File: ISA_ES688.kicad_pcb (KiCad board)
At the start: 4 copper layers, 104.1 x 99.1 mm, 105 parts, among them J1 LINE IN, J10 Vol. Btns, J11 ISA BUS, J2 MIC, J3 Joystick/MIDI, J5 Wavetable, J7 SPKR OUT, J8 LINE OUT, U1 L78L05, U2 74LS138, U3 ES1868F, U4 93LC66, U7 LM1877, Y1 14.318Mhz

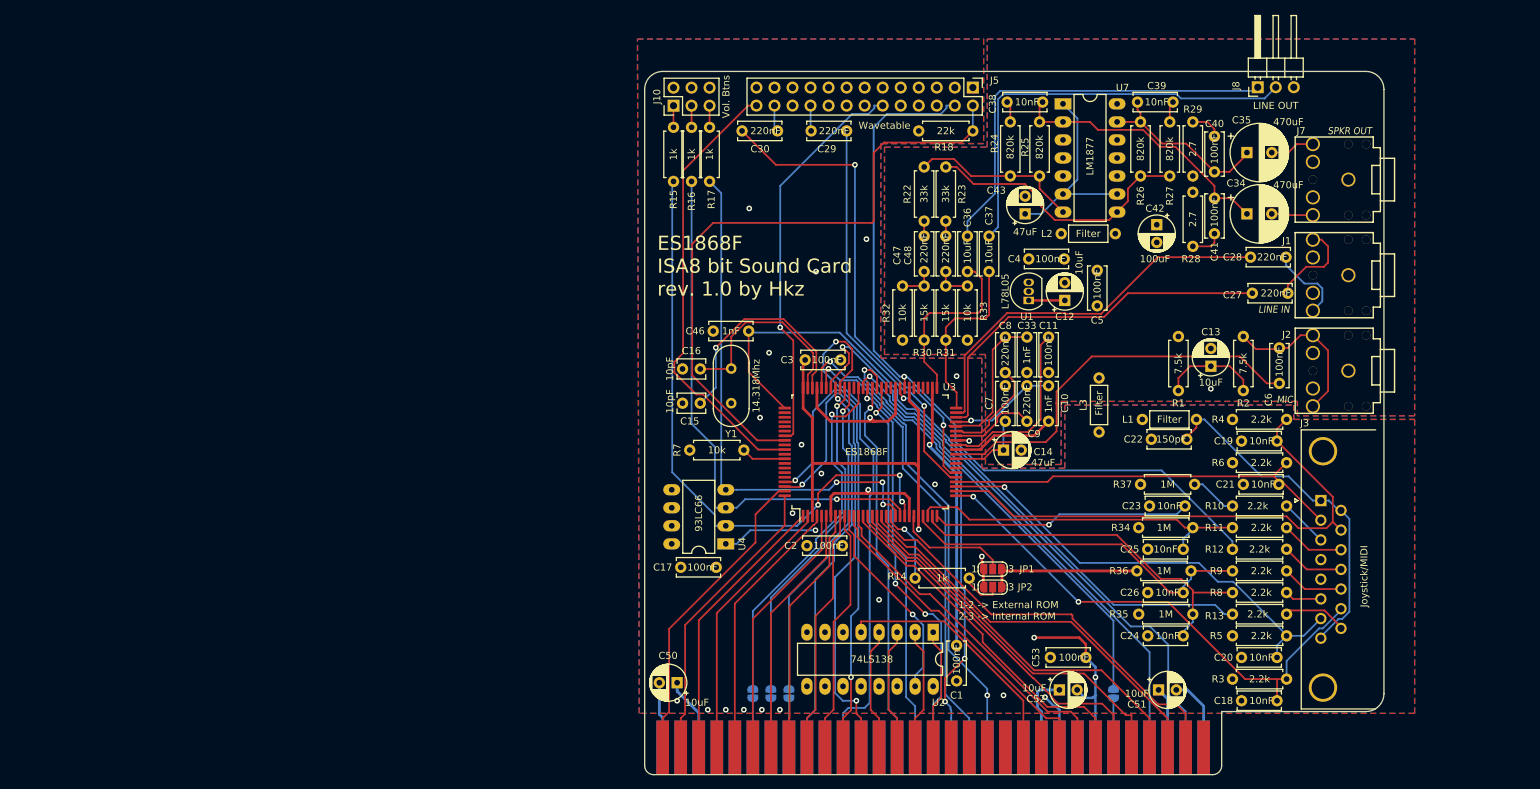
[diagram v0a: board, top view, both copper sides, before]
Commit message: Begin laying out parts
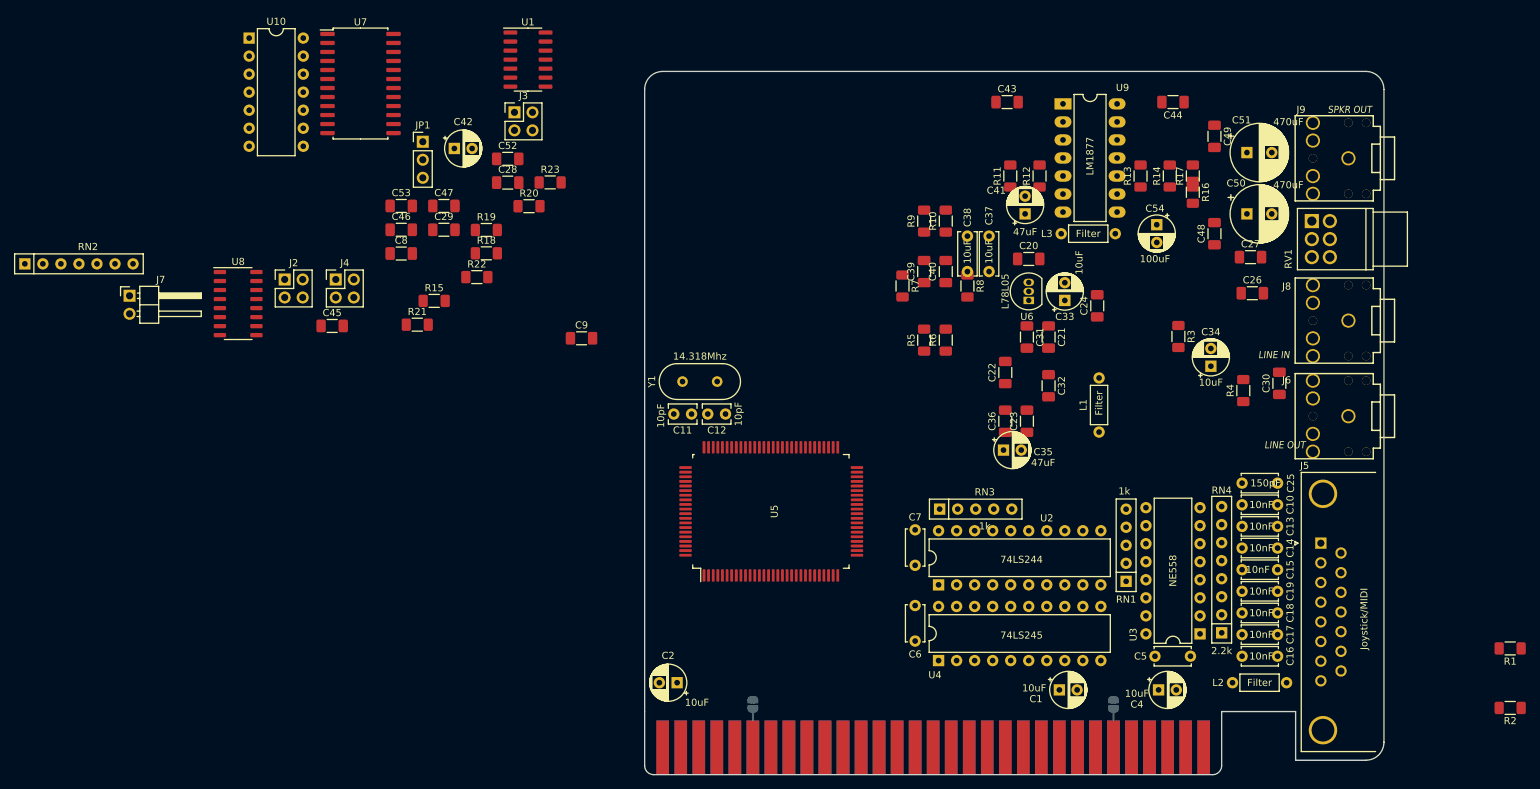
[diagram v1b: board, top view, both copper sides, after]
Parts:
- removed the C20 at (294.9, 186.7)
- removed the C21 at (295.1, 162.3)
- removed the C23 at (281.9, 165.4)
- removed the C24 at (281.7, 183.6)
- removed the C25 at (281.7, 171.4)
- removed the C26 at (281.7, 177.5)
- removed the C30 at (224.5, 112.5)
- removed J10: Vol. Btns, Connector_PinHeader_2.54mm:PinHeader_2x03_P2.54mm_Vertical
- removed the J5 at (257.0, 106.4)
- removed the J8 at (297.2, 106.4)
- removed JP4: ~DACK2~ Jumper, Jumper:SolderJumper-2_P1.3mm_Open_RoundedPad1.0x1.5mm
- removed JP5: IRQ3 Jumper, Jumper:SolderJumper-2_P1.3mm_Open_RoundedPad1.0x1.5mm
- removed JP6: IRQ4 Jumper, Jumper:SolderJumper-2_P1.3mm_Open_RoundedPad1.0x1.5mm
- removed the R10 at (301.2, 165.4)
- removed the R11 at (301.2, 168.4)
- removed the R14 at (256.5, 175.5)
- removed the R16 at (217.4, 119.6)
- removed the R17 at (220.0, 119.6)
- removed the R3 at (301.2, 189.7)
- removed R34, R35, R36, R37: 1M, Resistor_THT:R_Axial_DIN0207_L6.3mm_D2.5mm_P7.62mm_Horizontal
- removed the R4 at (301.2, 153.2)
- removed the R5 at (301.2, 183.6)
- removed the R6 at (301.2, 159.3)
- removed the R7 at (224.8, 157.5)
- removed the R8 at (301.2, 177.5)
- removed the R9 at (301.2, 174.5)
- added C10: 10nF, Capacitor_THT:C_Disc_D5.0mm_W2.5mm_P5.00mm, F.Cu at (300.0, 165.2)
- added C13: 10nF, Capacitor_THT:C_Disc_D5.0mm_W2.5mm_P5.00mm, F.Cu at (300.0, 168.2)
- added C14: 10nF, Capacitor_THT:C_Disc_D5.0mm_W2.5mm_P5.00mm, F.Cu at (300.0, 171.3)
- added C15: 10nF, Capacitor_THT:C_Disc_D5.0mm_W2.5mm_P5.00mm, F.Cu at (300.0, 174.3)
- added C16: 10nF, Capacitor_THT:C_Disc_D5.0mm_W2.5mm_P5.00mm, F.Cu at (300.0, 186.5)
- added C28: 220nF, Capacitor_SMD:C_1206_3216Metric_Pad1.33x1.80mm_HandSolder, F.Cu at (191.5, 119.8)
- added C42: 10uF, Capacitor_THT:CP_Radial_D5.0mm_P2.50mm, F.Cu at (184.0, 115.0)
- added C45: 2.7nF, Capacitor_SMD:C_1206_3216Metric_Pad1.33x1.80mm_HandSolder, F.Cu at (166.8, 140.0)
- added C46: 2.7nF, Capacitor_SMD:C_1206_3216Metric_Pad1.33x1.80mm_HandSolder, F.Cu at (176.5, 126.4)
- added C47: 33-68pF, Capacitor_SMD:C_1206_3216Metric_Pad1.33x1.80mm_HandSolder, F.Cu at (182.5, 123.1)
- added C52: 5nF, Capacitor_SMD:C_1206_3216Metric_Pad1.33x1.80mm_HandSolder, F.Cu at (191.5, 116.5)
- added C8: 10nF, Capacitor_SMD:C_1206_3216Metric_Pad1.33x1.80mm_HandSolder, F.Cu at (176.5, 129.8)
- added J2: Interrupt Select, Connector_PinHeader_2.54mm:PinHeader_2x02_P2.54mm_Vertical, F.Cu at (160.1, 133.4)
- added J3: Address Select, Connector_PinHeader_2.54mm:PinHeader_2x02_P2.54mm_Vertical, F.Cu at (192.5, 109.9)
- added J4: DMA Select, Connector_PinHeader_2.54mm:PinHeader_2x02_P2.54mm_Vertical, F.Cu at (167.3, 133.4)
- added J7: MIC, Connector_PinHeader_2.54mm:PinHeader_1x02_P2.54mm_Horizontal, F.Cu at (138.3, 135.7)
- added R19: 2.2k, Resistor_SMD:R_1206_3216Metric_Pad1.30x1.75mm_HandSolder, F.Cu at (188.5, 126.5)
- added R20: 10k, Resistor_SMD:R_1206_3216Metric_Pad1.30x1.75mm_HandSolder, F.Cu at (194.5, 123.1)
- added R21: 2.2k, Resistor_SMD:R_1206_3216Metric_Pad1.30x1.75mm_HandSolder, F.Cu at (178.8, 139.8)
- added R22: 10k, Resistor_SMD:R_1206_3216Metric_Pad1.30x1.75mm_HandSolder, F.Cu at (187.2, 133.1)
- added R23: 10k, Resistor_SMD:R_1206_3216Metric_Pad1.30x1.75mm_HandSolder, F.Cu at (197.5, 119.8)
- added RN1: 1k, Resistor_THT:R_Array_SIP5, F.Cu at (278.6, 176.0)
- added RN2: R_Network06, Resistor_THT:R_Array_SIP7, F.Cu at (123.5, 131.2)
- added RN3: 1k, Resistor_THT:R_Array_SIP5, F.Cu at (252.4, 165.8)
- added RN4: 2.2k, Resistor_THT:R_Array_SIP8, F.Cu at (292.1, 183.2)
- added RV1: Volume Knob, Volume_Pot:PTD902, F.Cu at (304.8, 125.2)
- added U1: 74LS14, Package_SO:SOIC-14_3.9x8.7mm_P1.27mm, F.Cu at (194.4, 102.5)
- added U10: LM3403, Package_DIP:DIP-14_W7.62mm, F.Cu at (155.1, 99.4)
- added U5: ES688F, Package_QFP:LQFP-14x20mm_P0.5mm, F.Cu at (228.6, 166.1)
- added U7: YMF262-M, Package_SO:SOIC-24W_7.5x15.4mm_P1.27mm, F.Cu at (170.8, 105.8)
- added U8: YAC512, Package_SO:SO-16_3.9x9.9mm_P1.27mm, F.Cu at (153.6, 136.8)
- C17: value 100nF -> 10nF; footprint Capacitor_THT:C_Disc_D6.0mm_W2.5mm_P5.00mm -> Capacitor_THT:C_Disc_D5.0mm_W2.5mm_P5.00mm
- C18, C19: footprint Capacitor_THT:C_Disc_D6.0mm_W2.5mm_P5.00mm -> Capacitor_THT:C_Disc_D5.0mm_W2.5mm_P5.00mm
- C20: renamed from C4; footprint Capacitor_THT:C_Disc_D6.0mm_W2.5mm_P5.00mm -> Capacitor_SMD:C_1206_3216Metric_Pad1.33x1.80mm_HandSolder
- C21: renamed from C11; footprint Capacitor_THT:C_Disc_D6.0mm_W2.5mm_P5.00mm -> Capacitor_SMD:C_1206_3216Metric_Pad1.33x1.80mm_HandSolder
- C22: renamed from C8; footprint Capacitor_THT:C_Disc_D6.0mm_W2.5mm_P5.00mm -> Capacitor_SMD:C_1206_3216Metric_Pad1.33x1.80mm_HandSolder
- C23: renamed from C9; footprint Capacitor_THT:C_Disc_D6.0mm_W2.5mm_P5.00mm -> Capacitor_SMD:C_1206_3216Metric_Pad1.33x1.80mm_HandSolder
- C24: renamed from C5; footprint Capacitor_THT:C_Disc_D6.0mm_W2.5mm_P5.00mm -> Capacitor_SMD:C_1206_3216Metric_Pad1.33x1.80mm_HandSolder
- C25: renamed from C22; footprint Capacitor_THT:C_Disc_D6.0mm_W2.5mm_P5.00mm -> Capacitor_THT:C_Disc_D5.0mm_W2.5mm_P5.00mm
- C26: renamed from C27; footprint Capacitor_THT:C_Disc_D6.0mm_W2.5mm_P5.00mm -> Capacitor_SMD:C_1206_3216Metric_Pad1.33x1.80mm_HandSolder
- C27: renamed from C28; footprint Capacitor_THT:C_Disc_D6.0mm_W2.5mm_P5.00mm -> Capacitor_SMD:C_1206_3216Metric_Pad1.33x1.80mm_HandSolder
- C29: footprint Capacitor_THT:C_Disc_D6.0mm_W2.5mm_P5.00mm -> Capacitor_SMD:C_1206_3216Metric_Pad1.33x1.80mm_HandSolder
- C30: renamed from C6; footprint Capacitor_THT:C_Disc_D6.0mm_W2.5mm_P5.00mm -> Capacitor_SMD:C_1206_3216Metric_Pad1.33x1.80mm_HandSolder
- C31: renamed from C33; footprint Capacitor_THT:C_Disc_D6.0mm_W2.5mm_P5.00mm -> Capacitor_SMD:C_1206_3216Metric_Pad1.33x1.80mm_HandSolder
- C32: renamed from C10; footprint Capacitor_THT:C_Disc_D6.0mm_W2.5mm_P5.00mm -> Capacitor_SMD:C_1206_3216Metric_Pad1.33x1.80mm_HandSolder
- C36: renamed from C7; footprint Capacitor_THT:C_Disc_D6.0mm_W2.5mm_P5.00mm -> Capacitor_SMD:C_1206_3216Metric_Pad1.33x1.80mm_HandSolder
- C39: renamed from C47; footprint Capacitor_THT:C_Disc_D6.0mm_W2.5mm_P5.00mm -> Capacitor_SMD:C_1206_3216Metric_Pad1.33x1.80mm_HandSolder
- C40: renamed from C48; footprint Capacitor_THT:C_Disc_D6.0mm_W2.5mm_P5.00mm -> Capacitor_SMD:C_1206_3216Metric_Pad1.33x1.80mm_HandSolder
- C43: renamed from C38; footprint Capacitor_THT:C_Disc_D6.0mm_W2.5mm_P5.00mm -> Capacitor_SMD:C_1206_3216Metric_Pad1.33x1.80mm_HandSolder
- C44: renamed from C39; footprint Capacitor_THT:C_Disc_D6.0mm_W2.5mm_P5.00mm -> Capacitor_SMD:C_1206_3216Metric_Pad1.33x1.80mm_HandSolder
- C48: renamed from C41; footprint Capacitor_THT:C_Disc_D6.0mm_W2.5mm_P5.00mm -> Capacitor_SMD:C_1206_3216Metric_Pad1.33x1.80mm_HandSolder
- C49: renamed from C40; footprint Capacitor_THT:C_Disc_D6.0mm_W2.5mm_P5.00mm -> Capacitor_SMD:C_1206_3216Metric_Pad1.33x1.80mm_HandSolder
- C5: renamed from C1; footprint Capacitor_THT:C_Disc_D6.0mm_W2.5mm_P5.00mm -> Capacitor_THT:C_Disc_D5.0mm_W2.5mm_P5.00mm
- C53: value 100nF -> 5nF; footprint Capacitor_THT:C_Disc_D6.0mm_W2.5mm_P5.00mm -> Capacitor_SMD:C_1206_3216Metric_Pad1.33x1.80mm_HandSolder
- C6: renamed from C2; footprint Capacitor_THT:C_Disc_D6.0mm_W2.5mm_P5.00mm -> Capacitor_THT:C_Disc_D5.0mm_W2.5mm_P5.00mm
- C7: renamed from C3; footprint Capacitor_THT:C_Disc_D6.0mm_W2.5mm_P5.00mm -> Capacitor_THT:C_Disc_D5.0mm_W2.5mm_P5.00mm
- C9: renamed from C46; footprint Capacitor_THT:C_Disc_D6.0mm_W2.5mm_P5.00mm -> Capacitor_SMD:C_1206_3216Metric_Pad1.33x1.80mm_HandSolder
- J6: renamed from J2; value MIC -> LINE OUT
- JP1: value Intl. ROM 1 -> Emulation Mode; footprint Jumper:SolderJumper-3_P1.3mm_Open_RoundedPad1.0x1.5mm_NumberLabels -> Connector_PinHeader_2.54mm:PinHeader_1x03_P2.54mm_Vertical
- JP2: value Intl. ROM 2 -> ~DRQ2~ Jumper; footprint Jumper:SolderJumper-3_P1.3mm_Open_RoundedPad1.0x1.5mm_NumberLabels -> Jumper:SolderJumper-2_P1.3mm_Open_RoundedPad1.0x1.5mm; moved to B.Cu
- JP3: value ~DRQ2~ Jumper -> ~DACK2~ Jumper
- R1: renamed from R12; footprint Resistor_THT:R_Axial_DIN0207_L6.3mm_D2.5mm_P7.62mm_Horizontal -> Resistor_SMD:R_1206_3216Metric_Pad1.30x1.75mm_HandSolder
- R10: renamed from R23; footprint Resistor_THT:R_Axial_DIN0207_L6.3mm_D2.5mm_P7.62mm_Horizontal -> Resistor_SMD:R_1206_3216Metric_Pad1.30x1.75mm_HandSolder
- R11: renamed from R24; footprint Resistor_THT:R_Axial_DIN0207_L6.3mm_D2.5mm_P7.62mm_Horizontal -> Resistor_SMD:R_1206_3216Metric_Pad1.30x1.75mm_HandSolder
- R12: renamed from R25; footprint Resistor_THT:R_Axial_DIN0207_L6.3mm_D2.5mm_P7.62mm_Horizontal -> Resistor_SMD:R_1206_3216Metric_Pad1.30x1.75mm_HandSolder
- R13: renamed from R26; footprint Resistor_THT:R_Axial_DIN0207_L6.3mm_D2.5mm_P7.62mm_Horizontal -> Resistor_SMD:R_1206_3216Metric_Pad1.30x1.75mm_HandSolder
- R14: renamed from R27; footprint Resistor_THT:R_Axial_DIN0207_L6.3mm_D2.5mm_P7.62mm_Horizontal -> Resistor_SMD:R_1206_3216Metric_Pad1.30x1.75mm_HandSolder
- R15: value 1k -> 33; footprint Resistor_THT:R_Axial_DIN0207_L6.3mm_D2.5mm_P7.62mm_Horizontal -> Resistor_SMD:R_1206_3216Metric_Pad1.30x1.75mm_HandSolder
- R16: renamed from R28; footprint Resistor_THT:R_Axial_DIN0207_L6.3mm_D2.5mm_P7.62mm_Horizontal -> Resistor_SMD:R_1206_3216Metric_Pad1.30x1.75mm_HandSolder
- R17: renamed from R29; footprint Resistor_THT:R_Axial_DIN0207_L6.3mm_D2.5mm_P7.62mm_Horizontal -> Resistor_SMD:R_1206_3216Metric_Pad1.30x1.75mm_HandSolder
- R18: value 22k -> 10k; footprint Resistor_THT:R_Axial_DIN0207_L6.3mm_D2.5mm_P7.62mm_Horizontal -> Resistor_SMD:R_1206_3216Metric_Pad1.30x1.75mm_HandSolder
- R2: renamed from R13; footprint Resistor_THT:R_Axial_DIN0207_L6.3mm_D2.5mm_P7.62mm_Horizontal -> Resistor_SMD:R_1206_3216Metric_Pad1.30x1.75mm_HandSolder
- R3: renamed from R1; footprint Resistor_THT:R_Axial_DIN0207_L6.3mm_D2.5mm_P7.62mm_Horizontal -> Resistor_SMD:R_1206_3216Metric_Pad1.30x1.75mm_HandSolder
- R4: renamed from R2; footprint Resistor_THT:R_Axial_DIN0207_L6.3mm_D2.5mm_P7.62mm_Horizontal -> Resistor_SMD:R_1206_3216Metric_Pad1.30x1.75mm_HandSolder
- R5: renamed from R30; footprint Resistor_THT:R_Axial_DIN0207_L6.3mm_D2.5mm_P7.62mm_Horizontal -> Resistor_SMD:R_1206_3216Metric_Pad1.30x1.75mm_HandSolder
- R6: renamed from R31; footprint Resistor_THT:R_Axial_DIN0207_L6.3mm_D2.5mm_P7.62mm_Horizontal -> Resistor_SMD:R_1206_3216Metric_Pad1.30x1.75mm_HandSolder
- R7: renamed from R32; footprint Resistor_THT:R_Axial_DIN0207_L6.3mm_D2.5mm_P7.62mm_Horizontal -> Resistor_SMD:R_1206_3216Metric_Pad1.30x1.75mm_HandSolder
- R8: renamed from R33; footprint Resistor_THT:R_Axial_DIN0207_L6.3mm_D2.5mm_P7.62mm_Horizontal -> Resistor_SMD:R_1206_3216Metric_Pad1.30x1.75mm_HandSolder
- R9: renamed from R22; footprint Resistor_THT:R_Axial_DIN0207_L6.3mm_D2.5mm_P7.62mm_Horizontal -> Resistor_SMD:R_1206_3216Metric_Pad1.30x1.75mm_HandSolder
- U2: value 74LS138 -> 74LS244; footprint Package_DIP:DIP-16_W7.62mm_LongPads -> Package_DIP:DIP-20_W7.62mm
- U3: value ES1868F -> NE558; footprint Package_QFP:LQFP-14x20mm_P0.5mm -> Package_DIP:DIP-16_W7.62mm
- U4: value 93LC66 -> 74LS245; footprint Package_DIP:DIP-8_W7.62mm_LongPads -> Package_DIP:DIP-20_W7.62mm
- moved C53 111.4 mm to (176.5, 123.1)
- moved JP1 100.3 mm to (179.6, 114.0)
- moved C17 79.6 mm to (300.0, 183.5)
- moved R18 70.7 mm to (188.5, 129.8), turned to 0 degrees
- moved C29 58.4 mm to (182.5, 126.4), turned to 0 degrees
- moved U3 53.1 mm to (289.1, 183.4), turned to 180 degrees
- moved JP3 50.8 mm to (226.1, 193.3)
- moved L2 39.2 mm to (293.6, 190.2)
- moved R15 37.7 mm to (181.2, 136.5), turned to 0 degrees
- moved R1 34.5 mm to (332.7, 185.4)
- moved U4 34.2 mm to (252.2, 187.1), turned to 90 degrees
- moved R2 34.2 mm to (332.7, 193.8)
- moved C7 28.5 mm to (248.9, 168.7), turned to 270 degrees
- moved C5 28.2 mm to (282.7, 186.5), turned to 0 degrees
- moved JP2 23.7 mm to (276.9, 193.3), turned to 90 degrees
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- renumbered C52 to C1, C15 to C11, C16 to C12, C50 to C2, C12 to C33, C13 to C34, C14 to C35, C36 to C38, C51 to C4, C43 to C41, C34 to C50, C35 to C51, C42 to C54, J11 to J1, J3 to J5, J1 to J8, J7 to J9, L3 to L1, L1 to L2, L2 to L3, U1 to U6, U7 to U9
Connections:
- C11 pad 2: Net-(C15-Pad2) -> Net-(C11-Pad2)
- C12 pad 2: Net-(C16-Pad2) -> /ES_CLK
- C17 pad 1: GND -> Net-(C17-Pad1)
- C17 pad 2: VCC -> GND
- C18 pad 1: GND -> Net-(C18-Pad1)
- C18 pad 2: Net-(C18-Pad2) -> GND
- C19 pad 1: GND -> Net-(C19-Pad1)
- C19 pad 2: Net-(C19-Pad2) -> GND
- C21 pad 1: Net-(C11-Pad1) -> Net-(C21-Pad1)
- C22 pad 1: Net-(C8-Pad1) -> Net-(C22-Pad1)
- C22 pad 2: Net-(C33-Pad1) -> Net-(C22-Pad2)
- C23 pad 1: Net-(C9-Pad1) -> Net-(C23-Pad1)
- C23 pad 2: Net-(C10-Pad1) -> Net-(C23-Pad2)
- C24 pad 1: /VDDA -> VDDA
- C26 pad 1: Net-(C27-Pad1) -> Net-(C26-Pad1)
- C27 pad 1: Net-(C28-Pad1) -> Net-(C27-Pad1)
- C29 pad 2: /AUXBL -> /MUS_R
- C30 pad 1: Net-(C6-Pad1) -> Net-(C30-Pad1)
- C30 pad 2: Net-(C6-Pad2) -> Net-(C30-Pad2)
- C31 pad 1: Net-(C33-Pad1) -> Net-(C22-Pad2)
- C32 pad 1: Net-(C10-Pad1) -> Net-(C23-Pad2)
- C33 pad 1: /VDDA -> VDDA
- C35 pad 1: Net-(C14-Pad1) -> Net-(C35-Pad1)
- C36 pad 1: Net-(C14-Pad1) -> Net-(C35-Pad1)
- C38 pad 2: Net-(C36-Pad2) -> Net-(C38-Pad2)
- C39 pad 2: Net-(C47-Pad2) -> Net-(C39-Pad2)
- C40 pad 2: Net-(C48-Pad2) -> Net-(C40-Pad2)
- C53 pad 1: GND -> /MUS_L
- C53 pad 2: -12V -> GNDA
- J1 pad 24: /IRQ4 -> (no net)
- J1 pad 47: /A15 -> (no net)
- J1 pad 48: /A14 -> (no net)
- J1 pad 49: /A13 -> (no net)
- J1 pad 50: /A12 -> (no net)
- J1 pad 51: /A11 -> (no net)
- J1 pad 52: /A10 -> (no net)
- J5 pad 10: Net-(C19-Pad2) -> Net-(C18-Pad1)
- J5 pad 14: Net-(C18-Pad2) -> Net-(C17-Pad1)
- J5 pad 2: Net-(C21-Pad2) -> Net-(C19-Pad1)
- J5 pad 7: Net-(C20-Pad2) -> Net-(C16-Pad1)
- J6 pad 2: Net-(C6-Pad2) -> Net-(C37-Pad2)
- J6 pad 3: Net-(C6-Pad2) -> Net-(C38-Pad2)
- JP1 pad 1: VCC -> GND
- JP1 pad 3: GND -> VCC
- JP2 pad 1: VCC -> /DRQ2
- JP3 pad 1: /DRQ2 -> /~DACK2
- R1 pad 2: /MSO -> /MIDI_OUT
- R10 pad 1: Net-(C48-Pad2) -> Net-(R10-Pad1)
- R15 pad 1: Net-(R15-Pad1) -> /YAC_SWIN
- R18 pad 1: /MCLK -> Net-(R18-Pad1)
- R18 pad 2: GND -> Net-(R18-Pad2)
- R2 pad 2: /MSI -> /MIDI_IN
- R3 pad 1: /VDDA -> VDDA
- R4 pad 2: Net-(C6-Pad2) -> Net-(C30-Pad2)
- R9 pad 1: Net-(C47-Pad2) -> Net-(R9-Pad1)
- U2 pad 1: /A15 -> /~JOY_R
- U2 pad 10: (no net) -> GND
- U2 pad 11: (no net) -> Net-(C19-Pad1)
- U2 pad 12: (no net) -> /D3
- U2 pad 13: (no net) -> Net-(C16-Pad1)
- U2 pad 14: (no net) -> /D2
- U2 pad 15: Net-(U2-Pad15) -> Net-(C18-Pad1)
- U2 pad 16: VCC -> /D1
- U2 pad 2: /A14 -> Net-(RN1-Pad2)
- U2 pad 3: /A13 -> /D7
- U2 pad 4: /A12 -> Net-(RN1-Pad5)
- U2 pad 5: /AEN -> /D6
- U2 pad 6: VCC -> Net-(RN1-Pad4)
- U2 pad 7: (no net) -> /D5
- U2 pad 8: GND -> Net-(RN1-Pad3)
- U2 pad 9: (no net) -> /D4
- U3 pad 1: /A2 -> Net-(RN1-Pad3)
- U3 pad 10: /A9 -> Net-(C13-Pad1)
- U3 pad 11: Net-(U2-Pad15) -> /~JOY_W
- U3 pad 12: /D0 -> GND
- U3 pad 13: /D1 -> Net-(U1-Pad2)
- U3 pad 14: /D2 -> /~JOY_W
- U3 pad 15: /D3 -> Net-(C10-Pad1)
- U3 pad 16: /D4 -> Net-(RN1-Pad2)
- U3 pad 2: /A3 -> Net-(C15-Pad1)
- U3 pad 3: VCC -> /~JOY_W
- U3 pad 4: /A4 -> Net-(C8-Pad2)
- U3 pad 5: /A5 -> VCC
- U3 pad 6: /A6 -> /~JOY_W
- U3 pad 7: GND -> Net-(C14-Pad1)
- U3 pad 8: /A7 -> Net-(RN1-Pad4)
- U3 pad 9: /A8 -> Net-(RN1-Pad5)
- U4 pad 1: Net-(R14-Pad2) -> /~IOR
- U4 pad 2: Net-(R15-Pad1) -> /D0
- U4 pad 3: Net-(R16-Pad1) -> /D1
- U4 pad 4: Net-(R17-Pad1) -> /D2
- U4 pad 5: GND -> /D3
- U4 pad 6: GND -> /D4
- U4 pad 7: (no net) -> /D5
- U4 pad 8: VCC -> /D6
- U6 pad 1: /VDDA -> VDDA
- Y1 pad 1: Net-(C15-Pad2) -> Net-(C11-Pad2)
- Y1 pad 2: Net-(C16-Pad2) -> /ES_CLK
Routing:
- net GND: track 702.1 -> 0.00 mm, vias 21 -> 0
- net VCC: track 385.7 -> 0.00 mm, vias 2 -> 0
- net GNDA: track 301.7 -> 0.00 mm, vias 1 -> 0
- net -12V: track 148.1 -> 0.00 mm, vias 2 -> 0
- net +12V: track 128.3 -> 0.00 mm, vias 1 -> 0
- net /MSO: track 110.1 -> 0.00 mm, vias 1 -> 0
- net /RESETDRV: track 106.8 -> 0.00 mm
- net /MCLK: track 90.7 -> 0.00 mm
- net Net-(R15-Pad1): track 87.3 -> 0.00 mm, vias 3 -> 0
- net /IRQ9: track 82.7 -> 0.00 mm, vias 1 -> 0
- net Net-(C19-Pad2): track 75.5 -> 0.00 mm
- net Net-(R16-Pad1): track 75.4 -> 0.00 mm, vias 1 -> 0
- net /IRQ7: track 74.0 -> 0.00 mm, vias 1 -> 0
- net Net-(C18-Pad2): track 74.0 -> 0.00 mm, vias 2 -> 0
- net Net-(R17-Pad1): track 73.0 -> 0.00 mm, vias 3 -> 0
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- removed copper zone on B.Cu, net GND
- removed copper zone on F.Cu, net GND
- removed copper zone on In1.Cu, net GND
- removed copper zone on B.Cu, net GNDA
- removed copper zone on F.Cu, net GNDA
- removed copper zone on In1.Cu, net GNDA
- removed copper zone on In2.Cu, net GNDA
- removed copper zone on In2.Cu, net VCC
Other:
- outline, holes or cut-outs redrawn
- board text removed: "1-2 -> External ROM 2-3 -> Internal ROM"
- board text removed: "ES1868F ISA8 bit Sound Card rev. 1.0 by Hkz"

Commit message: Begin placing some components on the board
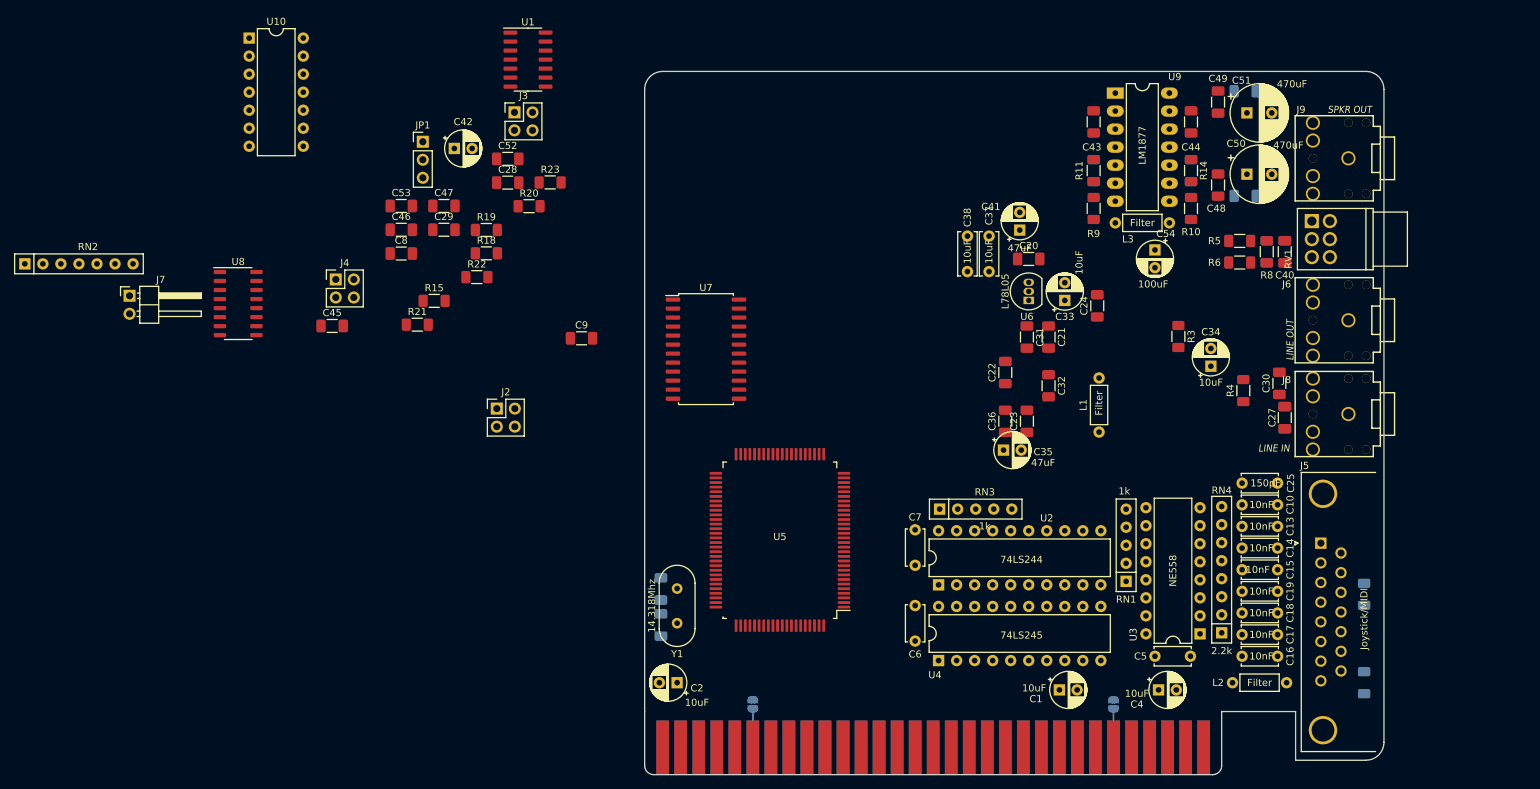
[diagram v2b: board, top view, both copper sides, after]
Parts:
- C11, C12: footprint Capacitor_THT:C_Disc_D3.8mm_W2.6mm_P2.50mm -> Capacitor_SMD:C_1206_3216Metric_Pad1.33x1.80mm_HandSolder; moved to B.Cu
- C26, C39, R1, R12, R13, R16, R17, R2, R7: moved to B.Cu
- moved U7 61.4 mm to (219.5, 143.3)
- moved R7 51.5 mm to (298.4, 129.5)
- moved C39 50.9 mm to (301.0, 129.5), turned to 270 degrees
- moved C40 47.8 mm to (301.0, 129.5), turned to 270 degrees
- moved R5 46.6 mm to (294.6, 128.0), turned to 0 degrees
- moved R6 42.8 mm to (294.6, 131.1), turned to 0 degrees
- moved R8 42.4 mm to (298.4, 129.5)
- moved J2 35.0 mm to (190.0, 151.6)
- moved R10 34.6 mm to (287.8, 123.4)
- moved Y1 34.0 mm to (215.4, 181.9), turned to 90 degrees
- moved C11 30.0 mm to (213.1, 182.1), turned to 270 degrees
- moved C12 25.5 mm to (213.1, 177.0), turned to 90 degrees
- moved R9 23.9 mm to (274.1, 123.4)
- moved C27 23.1 mm to (301.0, 152.9), turned to 270 degrees
- moved R1 21.9 mm to (312.2, 177.8), turned to 90 degrees
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
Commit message: More placing on PCB
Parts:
- moved C38 40.2 mm to (294.9, 143.5), turned to 0 degrees
- moved C37 35.7 mm to (294.9, 135.1), turned to 0 degrees
- moved C34 6.21 mm to (286.5, 150.4)
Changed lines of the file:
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@@
   )
   (module Capacitor_THT:C_Disc_D6.0mm_W2.5mm_P5.00mm (layer F.Cu)
-    (at 259.334 132.334 90)
+    (at 294.894 135.128)
     (descr "C, Disc series, Radial, pin pitch=5.00mm, , diameter*width=6*2.5mm^2, Capacitor, http://cdn-reichelt.de/documents/datenblatt/B300/DS_KERKO_TC.pdf")
     (tags "C Disc series Radial pin pitch 5.00mm  diameter 6mm width 2.5mm Capacitor")
-    (fp_text reference C37 (at 7.874 0 90) (layer F.SilkS)
-      (effects (font (size 1 1) (thickness 0.15)))
-    )
-    (fp_text value 10uF (at 2.794 0 90) (layer F.SilkS)
+    (fp_text reference C37 (at 2.54 2.286) (layer F.SilkS)
+      (effects (font (size 1 1) (thickness 0.15)))
+    )
+    (fp_text value 10uF (at 2.794 0) (layer F.SilkS)
       (effects (font (size 1 1) (thickness 0.15)))
     )
@@
     (fp_line (start 6.05 1.5) (end 6.05 -1.5) (layer F.CrtYd) (width 0.05))
     (fp_line (start 6.05 -1.5) (end -1.05 -1.5) (layer F.CrtYd) (width 0.05))
-    (fp_text user %R (at 2.5 0 90) (layer F.Fab)
-      (effects (font (size 1 1) (thickness 0.15)))
-    )
-    (pad 2 thru_hole circle (at 5 0 90) (size 1.6 1.6) (drill 0.8) (layers *.Cu *.Mask)
+    (fp_text user %R (at 2.5 0) (layer F.Fab)
+      (effects (font (size 1 1) (thickness 0.15)))
+    )
+    (pad 2 thru_hole circle (at 5 0) (size 1.6 1.6) (drill 0.8) (layers *.Cu *.Mask)
       (net 62 "Net-(C37-Pad2)"))
-    (pad 1 thru_hole circle (at 0 0 90) (size 1.6 1.6) (drill 0.8) (layers *.Cu *.Mask)
+    (pad 1 thru_hole circle (at 0 0) (size 1.6 1.6) (drill 0.8) (layers *.Cu *.Mask)
       (net 20 /AOUTL))
     (model ${KISYS3DMOD}/Capacitor_THT.3dshapes/C_Disc_D6.0mm_W2.5mm_P5.00mm.wrl
@@
   )
   (module Capacitor_THT:C_Disc_D6.0mm_W2.5mm_P5.00mm (layer F.Cu)
-    (at 256.286 132.334 90)
+    (at 294.894 143.51)
     (descr "C, Disc series, Radial, pin pitch=5.00mm, , diameter*width=6*2.5mm^2, Capacitor, http://cdn-reichelt.de/documents/datenblatt/B300/DS_KERKO_TC.pdf")
     (tags "C Disc series Radial pin pitch 5.00mm  diameter 6mm width 2.5mm Capacitor")
-    (fp_text reference C38 (at 7.62 0 90) (layer F.SilkS)
-      (effects (font (size 1 1) (thickness 0.15)))
-    )
-    (fp_text value 10uF (at 2.794 0 90) (layer F.SilkS)
+    (fp_text reference C38 (at 2.794 -2.286) (layer F.SilkS)
+      (effects (font (size 1 1) (thickness 0.15)))
+    )
+    (fp_text value 10uF (at 2.794 0) (layer F.SilkS)
       (effects (font (size 1 1) (thickness 0.15)))
     )
@@
     (fp_line (start 6.05 1.5) (end 6.05 -1.5) (layer F.CrtYd) (width 0.05))
     (fp_line (start 6.05 -1.5) (end -1.05 -1.5) (layer F.CrtYd) (width 0.05))
-    (fp_text user %R (at 2.5 0 90) (layer F.Fab)
-      (effects (font (size 1 1) (thickness 0.15)))
-    )
-    (pad 2 thru_hole circle (at 5 0 90) (size 1.6 1.6) (drill 0.8) (layers *.Cu *.Mask)
+    (fp_text user %R (at 2.5 0) (layer F.Fab)
+      (effects (font (size 1 1) (thickness 0.15)))
+    )
+    (pad 2 thru_hole circle (at 5 0) (size 1.6 1.6) (drill 0.8) (layers *.Cu *.Mask)
       (net 80 "Net-(C38-Pad2)"))
-    (pad 1 thru_hole circle (at 0 0 90) (size 1.6 1.6) (drill 0.8) (layers *.Cu *.Mask)
+    (pad 1 thru_hole circle (at 0 0) (size 1.6 1.6) (drill 0.8) (layers *.Cu *.Mask)
       (net 19 /AOUTR))
     (model ${KISYS3DMOD}/Capacitor_THT.3dshapes/C_Disc_D6.0mm_W2.5mm_P5.00mm.wrl
@@
   )
   (module Capacitor_THT:CP_Radial_D5.0mm_P2.50mm (layer F.Cu)
-    (at 290.576 145.666 90)
+    (at 286.512 150.368 90)
     (descr "CP, Radial series, Radial, pin pitch=2.50mm, , diameter=5mm, Electrolytic Capacitor")
     (tags "CP Radial series Radial pin pitch 2.50mm  diameter 5mm Electrolytic Capacitor")

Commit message: More placements
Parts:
- moved C41 21.6 mm to (270.3, 105.9), turned to 270 degrees
- moved C54 0.92 mm to (281.9, 129.8), turned to 180 degrees
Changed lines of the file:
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@@
     (descr "Inductor, Axial series, Axial, Horizontal, pin pitch=7.62mm, , length*diameter=5.3*2.2mm^2, Vishay, IM-1, http://www.vishay.com/docs/34030/im.pdf")
     (tags "Inductor Axial series Axial Horizontal pin pitch 7.62mm  length 5.3mm diameter 2.2mm Vishay IM-1")
-    (fp_text reference L3 (at 1.778 2.286) (layer F.SilkS)
+    (fp_text reference L3 (at -1.016 2.286) (layer F.SilkS)
       (effects (font (size 1 1) (thickness 0.15)))
     )
@@
   )
   (module Capacitor_THT:CP_Radial_D5.0mm_P2.50mm (layer F.Cu)
-    (at 263.652 126.492 90)
+    (at 270.256 105.918 270)
     (descr "CP, Radial series, Radial, pin pitch=2.50mm, , diameter=5mm, Electrolytic Capacitor")
     (tags "CP Radial series Radial pin pitch 2.50mm  diameter 5mm Electrolytic Capacitor")
-    (fp_text reference C41 (at 3.302 -4.064) (layer F.SilkS)
-      (effects (font (size 1 1) (thickness 0.15)))
-    )
-    (fp_text value 47uF (at -2.54 0) (layer F.SilkS)
+    (fp_text reference C41 (at -0.762 -4.064) (layer F.SilkS)
+      (effects (font (size 1 1) (thickness 0.15)))
+    )
+    (fp_text value 47uF (at -0.762 4.064) (layer F.SilkS)
       (effects (font (size 1 1) (thickness 0.15)))
     )
@@
       (effects (font (size 1 1) (thickness 0.15)))
     )
-    (pad 2 thru_hole circle (at 2.5 0 90) (size 1.6 1.6) (drill 0.8) (layers *.Cu *.Mask)
+    (pad 2 thru_hole circle (at 2.5 0 270) (size 1.6 1.6) (drill 0.8) (layers *.Cu *.Mask)
       (net 5 GNDA))
-    (pad 1 thru_hole rect (at 0 0 90) (size 1.6 1.6) (drill 0.8) (layers *.Cu *.Mask)
+    (pad 1 thru_hole rect (at 0 0 270) (size 1.6 1.6) (drill 0.8) (layers *.Cu *.Mask)
       (net 23 "Net-(C41-Pad1)"))
     (model ${KISYS3DMOD}/Capacitor_THT.3dshapes/CP_Radial_D5.0mm_P2.50mm.wrl
@@
   )
   (module Capacitor_THT:CP_Radial_D5.0mm_P2.50mm (layer F.Cu)
-    (at 282.702 129.286 270)
+    (at 281.94 129.794 180)
     (descr "CP, Radial series, Radial, pin pitch=2.50mm, , diameter=5mm, Electrolytic Capacitor")
     (tags "CP Radial series Radial pin pitch 2.50mm  diameter 5mm Electrolytic Capacitor")
-    (fp_text reference C54 (at -2.286 -1.524) (layer F.SilkS)
-      (effects (font (size 1 1) (thickness 0.15)))
-    )
-    (fp_text value 100uF (at 4.826 0.254) (layer F.SilkS)
+    (fp_text reference C54 (at -3.302 -0.254) (layer F.SilkS)
+      (effects (font (size 1 1) (thickness 0.15)))
+    )
+    (fp_text value 100uF (at -3.81 1.27) (layer F.SilkS)
       (effects (font (size 1 1) (thickness 0.15)))
     )
@@
     (fp_line (start -1.554775 -1.475) (end -1.054775 -1.475) (layer F.SilkS) (width 0.12))
     (fp_line (start -1.304775 -1.725) (end -1.304775 -1.225) (layer F.SilkS) (width 0.12))
-    (fp_text user %R (at 1.25 0 90) (layer F.Fab)
-      (effects (font (size 1 1) (thickness 0.15)))
-    )
-    (pad 2 thru_hole circle (at 2.5 0 270) (size 1.6 1.6) (drill 0.8) (layers *.Cu *.Mask)
+    (fp_text user %R (at 1.25 0) (layer F.Fab)
+      (effects (font (size 1 1) (thickness 0.15)))
+    )
+    (pad 2 thru_hole circle (at 2.5 0 180) (size 1.6 1.6) (drill 0.8) (layers *.Cu *.Mask)
       (net 5 GNDA))
-    (pad 1 thru_hole rect (at 0 0 270) (size 1.6 1.6) (drill 0.8) (layers *.Cu *.Mask)
+    (pad 1 thru_hole rect (at 0 0 180) (size 1.6 1.6) (drill 0.8) (layers *.Cu *.Mask)
       (net 63 /Filtered_12V))
     (model ${KISYS3DMOD}/Capacitor_THT.3dshapes/CP_Radial_D5.0mm_P2.50mm.wrl

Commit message: More movement on PCB
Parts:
- C20, C30: moved to B.Cu
- J7: footprint Connector_PinHeader_2.54mm:PinHeader_1x02_P2.54mm_Horizontal -> Connector_PinHeader_2.54mm:PinHeader_1x02_P2.54mm_Vertical
- moved J7 110.7 mm to (245.1, 106.7), turned to 270 degrees
- moved C30 71.8 mm to (238.0, 112.3)
- moved R4 69.7 mm to (238.0, 109.2), turned to 270 degrees
- moved C34 67.7 mm to (233.9, 107.7), turned to 270 degrees
- moved R3 65.0 mm to (229.6, 109.2), turned to 90 degrees
- moved C24 64.7 mm to (216.2, 109.3)
- moved C33 56.3 mm to (220.2, 110.1)
- moved U6 46.7 mm to (226.1, 110.5)
- moved C20 41.3 mm to (229.6, 109.2), turned to 270 degrees
- moved C6 1.52 mm to (248.9, 180.9)
- moved C7 1.52 mm to (248.9, 170.2)
- moved L2 1.52 mm to (293.6, 191.8)
